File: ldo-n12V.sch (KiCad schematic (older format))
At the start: 8 parts

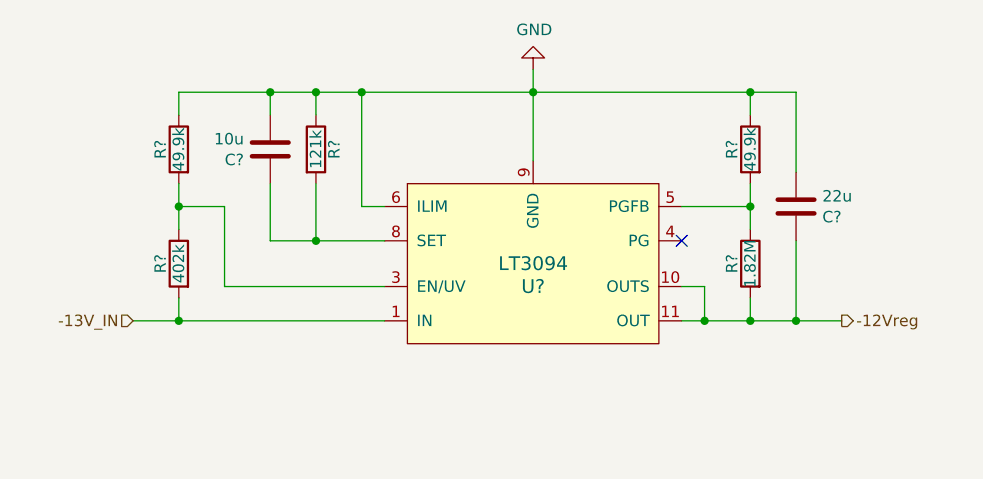
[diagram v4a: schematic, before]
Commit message: update resistor BOM for ldo sheets
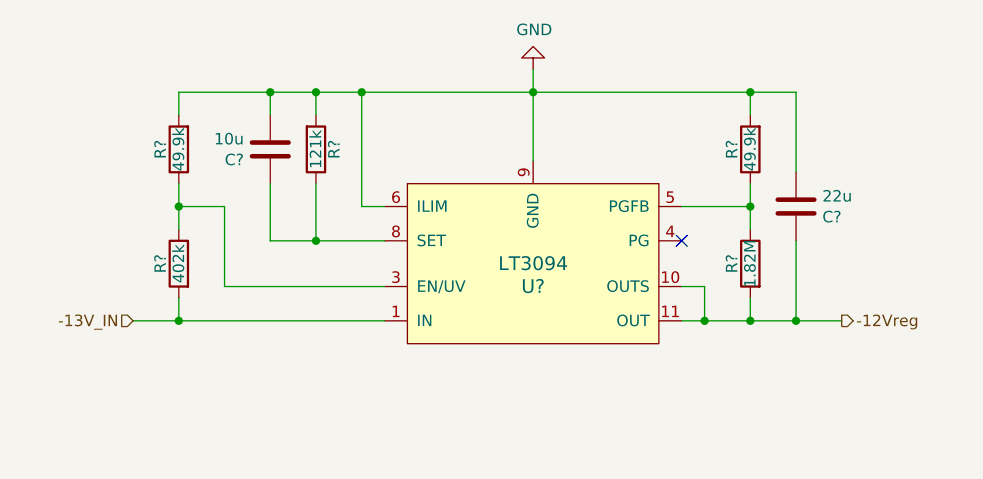
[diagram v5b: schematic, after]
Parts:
- removed R?: 121k, Resistor_SMD:R_0805_2012Metric_Pad1.15x1.40mm_HandSolder, symbol Device:R
- removed R? (x2): 49.9k, Resistor_SMD:R_0805_2012Metric_Pad1.15x1.40mm_HandSolder, symbol Device:R
- added R? (x2): 49.9k, Resistor_SMD:R_0805_2012Metric_Pad1.15x1.40mm_HandSolder, symbol Device:R
- added R?: 121k, Resistor_SMD:R_0805_2012Metric_Pad1.15x1.40mm_HandSolder, symbol Device:R
- R?: Description (none) -> RES SMD 1.82M OHM 1% 1/8W 0805; Manufacturer Part Number ERJ-6ENF1004V -> ERJ-6ENF1824V; Supplier Part Number P1.00MCCT-ND -> P1.82BTCT-ND
- R?: Description (none) -> RES SMD 402K OHM 1% 1/8W 0805; Manufacturer Part Number ERJ-6ENF1004V -> ERJ-6ENF4023V; Supplier Part Number P1.00MCCT-ND -> P402KCCT-ND
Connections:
- net GND: now also R?.2, R?.2, R?.2
- net at C?.2, U?.8 (SET): now also R?.1
- net at R?.1, U?.5 (PGFB): now also R?.1
- net at R?.1, U?.3 (EN/UV): now also R?.1
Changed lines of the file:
@@
 	5900 3700 5900 4000
-$Comp
-L Device:R R?
-U 1 1 5CA61ED4
-P 4950 3950
-AR Path="/5C87B3B6/5CA61ED4" Ref="R?"  Part="1"
-AR Path="/5CA59CF7/5CA61ED4" Ref="R?"  Part="1"
-AR Path="/5CA59CFA/5CA61ED4" Ref="R?"  Part="1"
-F 0 "R?" V 5030 3950 50  0000 C CNN
-F 1 "121k" V 4950 3950 50  0000 C CNN
-F 2 "Resistor_SMD:R_0805_2012Metric_Pad1.15x1.40mm_HandSolder" V 4880 3950 50  0001 C CNN
-F 3 "https://industrial.panasonic.com/cdbs/www-data/pdf/RDA0000/AOA0000C304.pdf" H 4950 3950 50  0001 C CNN
-F 4 "" H 4950 3950 50  0001 C CNN "Description"
-F 5 "Panasonic Electronic Components" H 4950 3950 50  0001 C CNN "Manufacturer"
-F 6 "ERJ-6ENF1004V" H 4950 3950 50  0001 C CNN "Manufacturer Part Number"
-F 7 "Digi-Key" H 4950 3950 50  0001 C CNN "Supplier"
-F 8 "P1.00MCCT-ND" H 4950 3950 50  0001 C CNN "Supplier Part Number"
-	1    4950 3950
-	1    0    0    -1
-$EndComp
 $Comp
 L Device:C C?
@@
 $Comp
 L Device:R R?
-U 1 1 5CA61EF7
-P 6850 3950
-AR Path="/5C87B3B6/5CA61EF7" Ref="R?"  Part="1"
-AR Path="/5CA59CF7/5CA61EF7" Ref="R?"  Part="1"
-AR Path="/5CA59CFA/5CA61EF7" Ref="R?"  Part="1"
-F 0 "R?" V 6930 3950 50  0000 C CNN
-F 1 "49.9k" V 6850 3950 50  0000 C CNN
-F 2 "Resistor_SMD:R_0805_2012Metric_Pad1.15x1.40mm_HandSolder" V 6780 3950 50  0001 C CNN
-F 3 "https://industrial.panasonic.com/cdbs/www-data/pdf/RDA0000/AOA0000C304.pdf" H 6850 3950 50  0001 C CNN
-F 4 "" H 6850 3950 50  0001 C CNN "Description"
-F 5 "Panasonic Electronic Components" H 6850 3950 50  0001 C CNN "Manufacturer"
-F 6 "ERJ-6ENF1004V" H 6850 3950 50  0001 C CNN "Manufacturer Part Number"
-F 7 "Digi-Key" H 6850 3950 50  0001 C CNN "Supplier"
-F 8 "P1.00MCCT-ND" H 6850 3950 50  0001 C CNN "Supplier Part Number"
-	1    6850 3950
-	-1   0    0    -1
-$EndComp
-$Comp
-L Device:R R?
 U 1 1 5CA61F03
 P 6850 4450
@@
 F 2 "Resistor_SMD:R_0805_2012Metric_Pad1.15x1.40mm_HandSolder" V 6780 4450 50  0001 C CNN
 F 3 "https://industrial.panasonic.com/cdbs/www-data/pdf/RDA0000/AOA0000C304.pdf" H 6850 4450 50  0001 C CNN
-F 4 "" H 6850 4450 50  0001 C CNN "Description"
+F 4 "RES SMD 1.82M OHM 1% 1/8W 0805" H 6850 4450 50  0001 C CNN "Description"
 F 5 "Panasonic Electronic Components" H 6850 4450 50  0001 C CNN "Manufacturer"
-F 6 "ERJ-6ENF1004V" H 6850 4450 50  0001 C CNN "Manufacturer Part Number"
+F 6 "ERJ-6ENF1824V" H 6850 4450 50  0001 C CNN "Manufacturer Part Number"
 F 7 "Digi-Key" H 6850 4450 50  0001 C CNN "Supplier"
-F 8 "P1.00MCCT-ND" H 6850 4450 50  0001 C CNN "Supplier Part Number"
+F 8 "P1.82BTCT-ND" H 6850 4450 50  0001 C CNN "Supplier Part Number"
 	1    6850 4450
 	-1   0    0    -1
@@
 $Comp
 L Device:R R?
-U 1 1 5CAC362A
-P 4350 3950
-AR Path="/5C87B3B6/5CAC362A" Ref="R?"  Part="1"
-AR Path="/5CA59CF7/5CAC362A" Ref="R?"  Part="1"
-AR Path="/5CA59CFA/5CAC362A" Ref="R?"  Part="1"
-F 0 "R?" V 4430 3950 50  0000 C CNN
-F 1 "49.9k" V 4350 3950 50  0000 C CNN
-F 2 "Resistor_SMD:R_0805_2012Metric_Pad1.15x1.40mm_HandSolder" V 4280 3950 50  0001 C CNN
-F 3 "https://industrial.panasonic.com/cdbs/www-data/pdf/RDA0000/AOA0000C304.pdf" H 4350 3950 50  0001 C CNN
-F 4 "" H 4350 3950 50  0001 C CNN "Description"
-F 5 "Panasonic Electronic Components" H 4350 3950 50  0001 C CNN "Manufacturer"
-F 6 "ERJ-6ENF1004V" H 4350 3950 50  0001 C CNN "Manufacturer Part Number"
-F 7 "Digi-Key" H 4350 3950 50  0001 C CNN "Supplier"
-F 8 "P1.00MCCT-ND" H 4350 3950 50  0001 C CNN "Supplier Part Number"
-	1    4350 3950
-	-1   0    0    -1
-$EndComp
-$Comp
-L Device:R R?
 U 1 1 5CAC3636
 P 4350 4450
@@
 F 2 "Resistor_SMD:R_0805_2012Metric_Pad1.15x1.40mm_HandSolder" V 4280 4450 50  0001 C CNN
 F 3 "https://industrial.panasonic.com/cdbs/www-data/pdf/RDA0000/AOA0000C304.pdf" H 4350 4450 50  0001 C CNN
-F 4 "" H 4350 4450 50  0001 C CNN "Description"
+F 4 "RES SMD 402K OHM 1% 1/8W 0805" H 4350 4450 50  0001 C CNN "Description"
 F 5 "Panasonic Electronic Components" H 4350 4450 50  0001 C CNN "Manufacturer"
-F 6 "ERJ-6ENF1004V" H 4350 4450 50  0001 C CNN "Manufacturer Part Number"
+F 6 "ERJ-6ENF4023V" H 4350 4450 50  0001 C CNN "Manufacturer Part Number"
 F 7 "Digi-Key" H 4350 4450 50  0001 C CNN "Supplier"
-F 8 "P1.00MCCT-ND" H 4350 4450 50  0001 C CNN "Supplier Part Number"
+F 8 "P402KCCT-ND" H 4350 4450 50  0001 C CNN "Supplier Part Number"
 	1    4350 4450
 	-1   0    0    -1
@@
 	4350 3700 4750 3700
 Connection ~ 4750 3700
+$Comp
+L Device:R R?
+U 1 1 5CAEF591
+P 4350 3950
+AR Path="/5C87B3B6/5CAEF591" Ref="R?"  Part="1"
+AR Path="/5CA59CF7/5CAEF591" Ref="R?"  Part="1"
+AR Path="/5CA59CFA/5CAEF591" Ref="R?"  Part="1"
+F 0 "R?" V 4430 3950 50  0000 C CNN
+F 1 "49.9k" V 4350 3950 50  0000 C CNN
+F 2 "Resistor_SMD:R_0805_2012Metric_Pad1.15x1.40mm_HandSolder" V 4280 3950 50  0001 C CNN
+F 3 "https://industrial.panasonic.com/cdbs/www-data/pdf/RDA0000/AOA0000C304.pdf" H 4350 3950 50  0001 C CNN
+F 4 "RES SMD 49.9K OHM 1% 1/8W 0805" H 4350 3950 50  0001 C CNN "Description"
+F 5 "Panasonic Electronic Components" H 4350 3950 50  0001 C CNN "Manufacturer"
+F 6 "ERJ-6ENF4992V" H 4350 3950 50  0001 C CNN "Manufacturer Part Number"
+F 7 "Digi-Key" H 4350 3950 50  0001 C CNN "Supplier"
+F 8 "P49.9KCCT-ND" H 4350 3950 50  0001 C CNN "Supplier Part Number"
+	1    4350 3950
+	-1   0    0    1
+$EndComp
+$Comp
+L Device:R R?
+U 1 1 5CAEFC49
+P 6850 3950
+AR Path="/5C87B3B6/5CAEFC49" Ref="R?"  Part="1"
+AR Path="/5CA59CF7/5CAEFC49" Ref="R?"  Part="1"
+AR Path="/5CA59CFA/5CAEFC49" Ref="R?"  Part="1"
+F 0 "R?" V 6930 3950 50  0000 C CNN
+F 1 "49.9k" V 6850 3950 50  0000 C CNN
+F 2 "Resistor_SMD:R_0805_2012Metric_Pad1.15x1.40mm_HandSolder" V 6780 3950 50  0001 C CNN
+F 3 "https://industrial.panasonic.com/cdbs/www-data/pdf/RDA0000/AOA0000C304.pdf" H 6850 3950 50  0001 C CNN
+F 4 "RES SMD 49.9K OHM 1% 1/8W 0805" H 6850 3950 50  0001 C CNN "Description"
+F 5 "Panasonic Electronic Components" H 6850 3950 50  0001 C CNN "Manufacturer"
+F 6 "ERJ-6ENF4992V" H 6850 3950 50  0001 C CNN "Manufacturer Part Number"
+F 7 "Digi-Key" H 6850 3950 50  0001 C CNN "Supplier"
+F 8 "P49.9KCCT-ND" H 6850 3950 50  0001 C CNN "Supplier Part Number"
+	1    6850 3950
+	-1   0    0    1
+$EndComp
+$Comp
+L Device:R R?
+U 1 1 5CAF0F36
+P 4950 3950
+AR Path="/5C87B3B6/5CAF0F36" Ref="R?"  Part="1"
+AR Path="/5CA59CF7/5CAF0F36" Ref="R?"  Part="1"
+AR Path="/5CA59CFA/5CAF0F36" Ref="R?"  Part="1"
+F 0 "R?" V 5030 3950 50  0000 C CNN
+F 1 "121k" V 4950 3950 50  0000 C CNN
+F 2 "Resistor_SMD:R_0805_2012Metric_Pad1.15x1.40mm_HandSolder" V 4880 3950 50  0001 C CNN
+F 3 "https://industrial.panasonic.com/cdbs/www-data/pdf/RDA0000/AOA0000C304.pdf" H 4950 3950 50  0001 C CNN
+F 4 "RES SMD 121K OHM 1% 1/8W 0805" H 4950 3950 50  0001 C CNN "Description"
+F 5 "Panasonic Electronic Components" H 4950 3950 50  0001 C CNN "Manufacturer"
+F 6 "ERJ-6ENF1213V" H 4950 3950 50  0001 C CNN "Manufacturer Part Number"
+F 7 "Digi-Key" H 4950 3950 50  0001 C CNN "Supplier"
+F 8 "P121KCCT-ND" H 4950 3950 50  0001 C CNN "Supplier Part Number"
+	1    4950 3950
+	1    0    0    1
+$EndComp
 $EndSCHEMATC

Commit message: replace LDO SET resistors with high-precision thin (metal) film variants
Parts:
- R?: Description RES SMD 121K OHM 1% 1/8W 0805 -> RES SMD 121K OHM 0.1% 1/8W 0805 Thin Film; Manufacturer Part Number ERJ-6ENF1213V -> ERA-6AEB1213V; Supplier Part Number P121KCCT-ND -> P121KDACT-ND
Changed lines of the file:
@@
 F 1 "121k" V 4950 3950 50  0000 C CNN
 F 2 "Resistor_SMD:R_0805_2012Metric_Pad1.15x1.40mm_HandSolder" V 4880 3950 50  0001 C CNN
-F 3 "https://industrial.panasonic.com/cdbs/www-data/pdf/RDA0000/AOA0000C304.pdf" H 4950 3950 50  0001 C CNN
-F 4 "RES SMD 121K OHM 1% 1/8W 0805" H 4950 3950 50  0001 C CNN "Description"
+F 3 "https://industrial.panasonic.com/cdbs/www-data/pdf/RDM0000/AOA0000C307.pdf" H 4950 3950 50  0001 C CNN
+F 4 "RES SMD 121K OHM 0.1% 1/8W 0805 Thin Film" H 4950 3950 50  0001 C CNN "Description"
 F 5 "Panasonic Electronic Components" H 4950 3950 50  0001 C CNN "Manufacturer"
-F 6 "ERJ-6ENF1213V" H 4950 3950 50  0001 C CNN "Manufacturer Part Number"
+F 6 "ERA-6AEB1213V" H 4950 3950 50  0001 C CNN "Manufacturer Part Number"
 F 7 "Digi-Key" H 4950 3950 50  0001 C CNN "Supplier"
-F 8 "P121KCCT-ND" H 4950 3950 50  0001 C CNN "Supplier Part Number"
+F 8 "P121KDACT-ND" H 4950 3950 50  0001 C CNN "Supplier Part Number"
 	1    4950 3950
 	1    0    0    1

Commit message: comments in negative LDO sheet
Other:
- note added: "EN/UV resistor divider sets IC enable threshold"
- note added: "PGFB resistor divider enables fast startup circuitry\nuntil the upper bound threshold set by the divider"
- note added: "SET resistor is high-precision thin (metal) film"
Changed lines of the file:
@@
 	1    0    0    1
 $EndComp
+Text Notes 5350 4950 0    50   ~ 0
+SET resistor is high-precision thin (metal) film
+Text Notes 5350 5300 0    50   ~ 0
+PGFB resistor divider enables fast startup circuitry\nuntil the upper bound threshold set by the divider
+Text Notes 5350 5100 0    50   ~ 0
+EN/UV resistor divider sets IC enable threshold
 $EndSCHEMATC

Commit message: BOM details for LDOs
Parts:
- U?: Description (none) -> 500mA Negative Linear Voltage Regulator; Manufacturer (none) -> Linear Technology; Manufacturer Part Number (none) -> LT3094EMSE#PBF; Supplier (none) -> Digi-Key; Supplier Part Number (none) -> LT3094EMSE#PBF-ND
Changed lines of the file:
@@
 F 2 "Housings_SSOP:MSOP-12-1EP_3x4mm_Pitch0.65mm" H 5900 3950 60  0001 C CNN
 F 3 "https://www.analog.com/media/en/technical-documentation/data-sheets/LT3094.pdf" H 5900 4050 60  0001 C CNN
+F 4 "500mA Negative Linear Voltage Regulator" H 0   0   50  0001 C CNN "Description"
+F 5 "Linear Technology" H 0   0   50  0001 C CNN "Manufacturer"
+F 6 "LT3094EMSE#PBF" H 0   0   50  0001 C CNN "Manufacturer Part Number"
+F 7 "Digi-Key" H 0   0   50  0001 C CNN "Supplier"
+F 8 "LT3094EMSE#PBF-ND" H 0   0   50  0001 C CNN "Supplier Part Number"
 	1    5900 4450
 	1    0    0    -1
